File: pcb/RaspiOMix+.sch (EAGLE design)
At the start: 103 parts, among them IC3 DS1307, IC4 MCP3424-E/ST, IC5 MCP3424-E/ST, IC6 TMP101, K1 PIN20X2, U1 EEPROM24

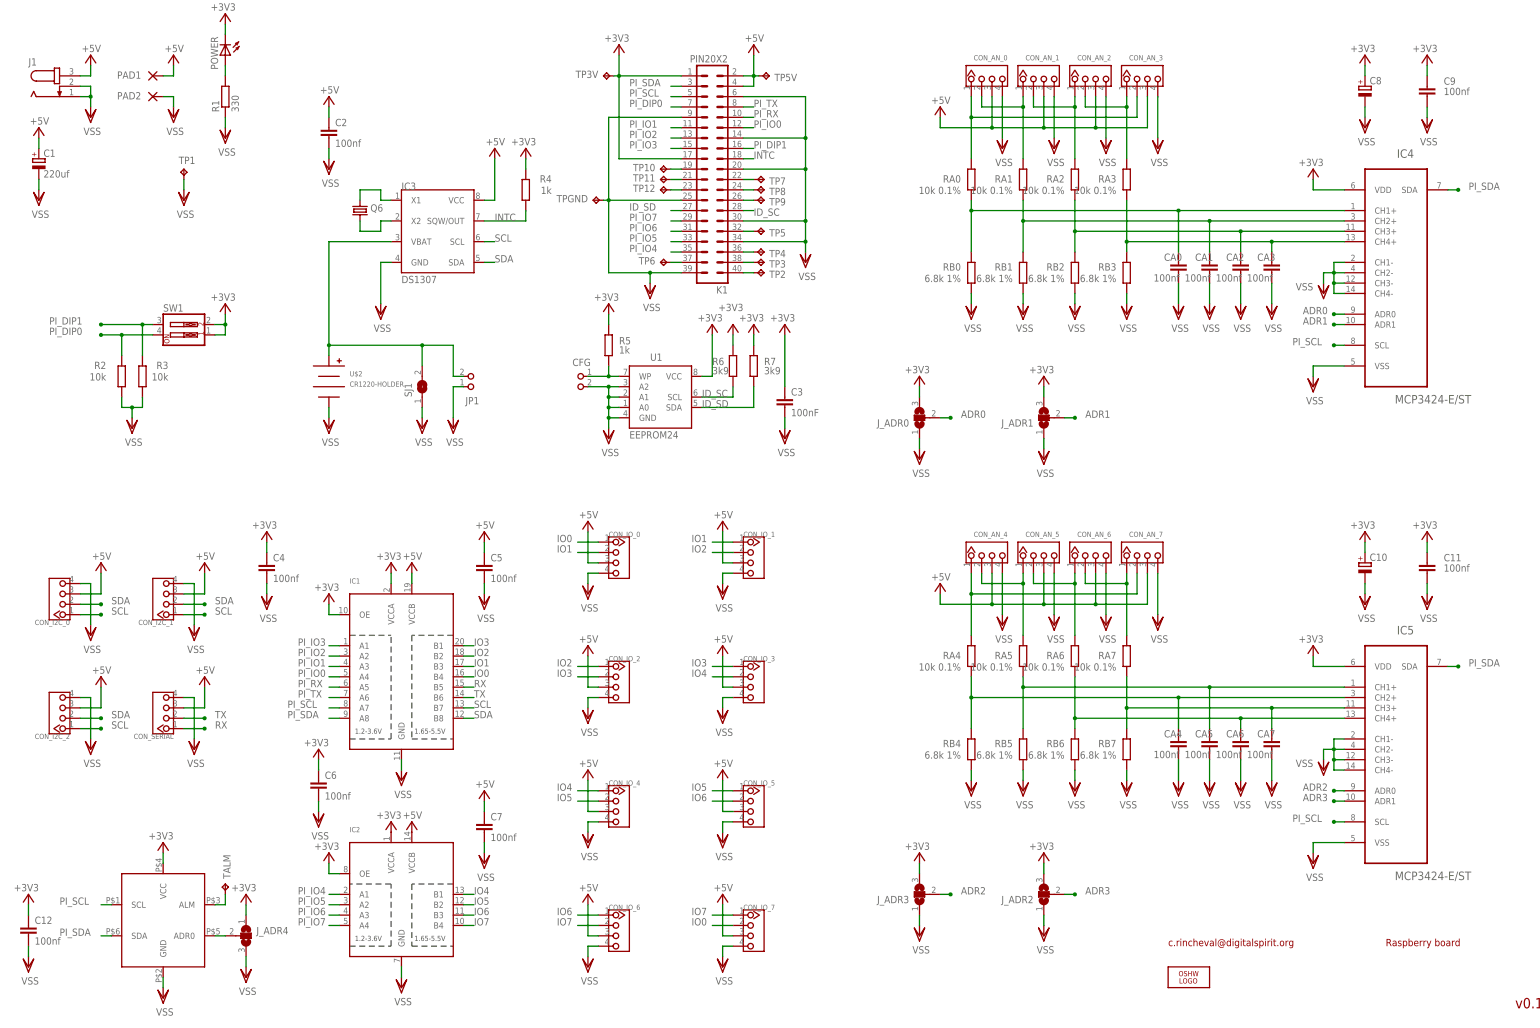
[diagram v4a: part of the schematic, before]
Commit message: RaspiO'Mix+ -> Pcb 2.0.0
New RaspiO’Mix+ pcbs version is 2.0.0.
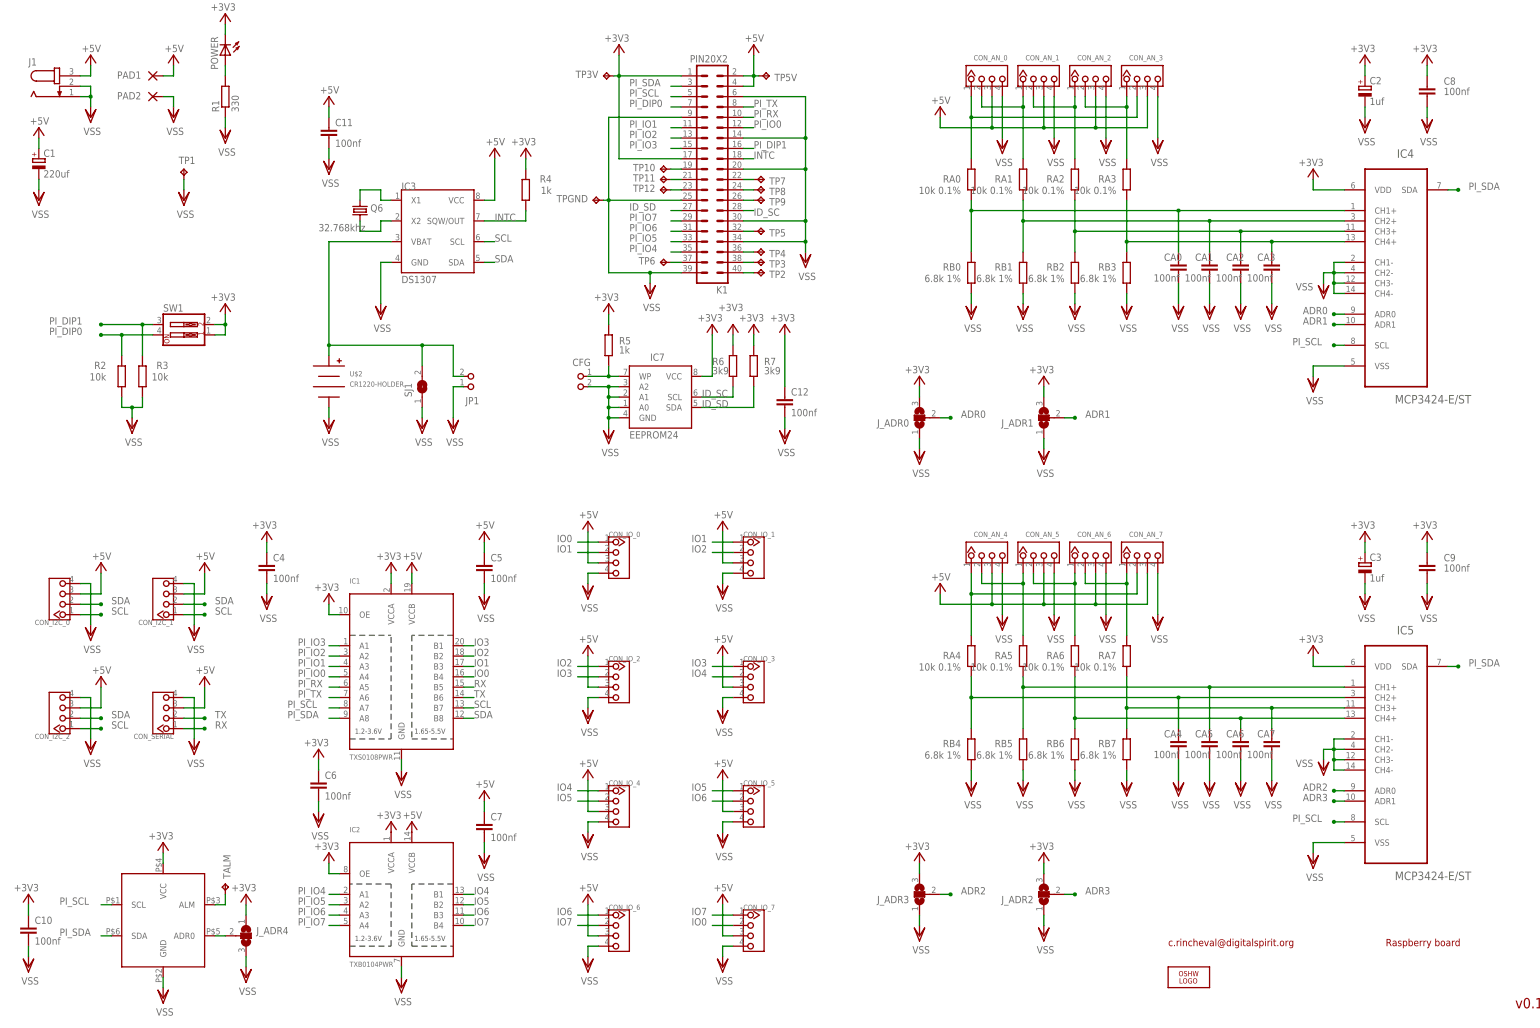
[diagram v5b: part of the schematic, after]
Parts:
- C10, C8: value (none) -> 100nf; device rcl:CPOL-EUB/3528-21R -> rcl:C-EUC0805
- C12: device rcl:C-EUC0805 -> resistor:C-EUC0805K; DIELECTRIC (none) -> X7R
- C2: value 100nf -> 1uf; device rcl:C-EUC0805 -> rcl:CPOL-EUB/3528-21R
- C3: value 100nF -> 1uf; device resistor:C-EUC0805K -> rcl:CPOL-EUB/3528-21R; DIELECTRIC X7R -> (none)
- IC1: value (none) -> TXS0108PWR
- IC2: value (none) -> TXB0104PWR
- Q6: value (none) -> 32.768khz
- renumbered U1 to IC7
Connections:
- net +3V3: now also C10.1, C2.+, C3.+, C8.2; no longer C10.+, C11.2, C3.1, C8.+
- net +5V: now also C11.1; no longer C2.1
- net VSS: now also C10.2, C11.2, C2.-, C3.-, C8.1; no longer C10.-, C11.1, C2.2, C3.2, C8.-
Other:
- moved on the sheet: C11, C12, C9
